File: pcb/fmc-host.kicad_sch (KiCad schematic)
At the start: 309 parts, among them J1 SMA002, J10 BM08B-SURS-TF, J2 SMA002, J3 SMA002, J4 SMA002, J5 SMA002, J6 FTSH-105-01-F-D-RA-K, J7 12226-8250-00FR, J8 FMC_SINGLE_WIDTH_MODULE, J9 ASP-134488-01, Q1 SI1012R, Q2 SI1012R, U1 SN74LVC2G34DCKR, U10 DS90UB934-Q1, U11 DS91M040, U12 AD5766BCPZ-RL7, U13 MCP47FEB02A0-E/ST, U14 LM4132AMF-2.5/NOPBCT-ND, U15 AD7616BSTZ, U16 AD5142BCPZ10, U17 LTM4622A, U18 D3V3XA4B10LP, U19 TPS7A49, U2 SN65LVDS9638DGN, U20 TPS7A49, U21 TPS7A30, U22 24ST, U23 LTM8049_BGA, U24 TPS62061DSGT, U25 D3V3XA4B10LP, U26 D3V3XA4B10LP, U3 FIN1032MTCX, U4 ADCMP600, U5 ADCMP600, U6 DG1412E, U7 DG1412E, U8 DG1412E, U9 DS90UB934-Q1, X2 OE-LOGO_7X5

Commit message: Added OEPS PN
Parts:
- C1, C106, C118, C139, C140, C2, C26, C27, C34, C35, C36, C37, C5, C6, C70, C71, C72, C73, C79, C80, C81, C91, C92: MPN (none) -> GRM31CR71E106KA12L; OEPS PN (none) -> OEPS M05 035; old description (none) -> CAP CER 1206 10uF 25V ±10% X7R
- C10, C100, C104, C107, C110, C111, C112, C114, C115, C13, C132, C134, C135, C137, C138, C14, C15, C16, C17, C18, C19, C22, C23, C3, C30, C31, C32, C33, C4, C41, C43, C44, C45, C46, C47, C48, C49, C52, C53, C54, C55, C56, C60, C61, C63, C65, C67, C68, C7, C78, C8, C83, C84, C85, C86, C87, C89, C9, C90, C93, C99: MPN (none) -> GRM155R71E104KE14D; OEPS PN (none) -> OEPS M05 032; old description (none) -> CAP CER 0402 100nF 25V ±10% X7R
- C101, C103, C105, C108, C109, C113, C116, C117, C119, C120, C121, C125, C126, C127, C59, C62, C69, C77, C95, C96: MPN (none) -> GRM21BR61E106KA73L; OEPS PN (none) -> OEPS M05 034; old description (none) -> CAP CER 0805 10uF 25V ±10% X5R
- C102, C130, C131, C94, C97, C98: MPN (none) -> TMK325ABJ476MM-T; OEPS PN (none) -> OEPS M05 036; old description (none) -> CAP CER 1210 47uF 25V ±20% X5R
- C11, C12, C122, C123, C124, C20, C21, C24, C25, C50, C51, C57, C58, C82: MPN (none) -> GCM155R71E103KA37D; OEPS PN (none) -> OEPS M05 030; old description (none) -> CAP CER 0402 10nF 25V ±10% X7R
- C128, C129: MPN (none) -> C1210C104KCRAC7800; OEPS PN (none) -> OEPS M05 072; old description (none) -> CAP CER 1210 100nF 500V ±10% X7R
- C133, C136: MPN (none) -> TL8B0336M020C; OEPS PN (none) -> OEPS M05 073; old description (none) -> CAP TAN 1411 33uF 20V ±20% B0
- C28, C29: MPN (none) -> CC0402KRX7R8BB472; OEPS PN (none) -> OEPS M05 029; old description (none) -> CAP CER 0402 4.7nF 25V ±10% X7R
- C38, C39: MPN (none) -> GRM155R71E473KA88D; OEPS PN (none) -> OEPS M05 031; old description (none) -> CAP CER 0402 47nF 25V ±10% X7R
- C40, C42, C64, C66, C74, C75, C76, C88: MPN (none) -> GCM21BR71E105KA56L; OEPS PN (none) -> OEPS M05 033; old description (none) -> CAP CER 0805 1uF 25V ±10% X7R
- D1, D2: MPN (none) -> SESD0402X1UN-0030-088; OEPS PN (none) -> OEPS M05 043; old description (none) -> TVS Diode 0402
- D3, D4, D5: MPN (none) -> BAR 66 E6327; OEPS PN (none) -> OEPS M05 044; old description (none) -> PIN Diode STO23
- D6: MPN (none) -> KDZVTR4.3B; OEPS PN (none) -> OEPS M05 045; old description (none) -> Zener Diode SOD123
- F1, F2, F3: MPN (none) -> MINISMDC014F-2; OEPS PN (none) -> OEPS M05 008; old description (none) -> Polyfuse
- J1, J2, J3, J4, J5: MPN (none) -> 6-1634010-0; OEPS PN (none) -> OEPS M05 001; old description (none) -> MMCX Coax Connector
- J10: MPN (none) -> BM08B-SURS-TF; OEPS PN (none) -> OEPS M05 076; old description (none) -> Connector header 8POS 0.8mm
- J6: MPN (none) -> FTSH-105-01-F-D-RA-K; OEPS PN (none) -> OEPS M05 077; old description (none) -> Connector header RA 10POS 1.27mm
- J7: MPN (none) -> 12226-8250-00FR; OEPS PN (none) -> OEPS M05 003; old description (none) -> SDR Cable Receptacle
- J8, TP1, TP10, TP11, TP12, TP13, TP14, TP15, TP16, TP17, TP18, TP2, TP3, TP4, TP5, TP6, TP7, TP8, TP9, X2: now not fitted; now left out of the parts list
- J9: MPN (none) -> ASP-134488-01; OEPS PN (none) -> OEPS M05 005; old description (none) -> FMC HPC Male Connector
- L1, L2: MPN (none) -> 1008PS-472KLB; OEPS PN (none) -> OEPS M05 037; old description (none) -> Inductor
- L10, L11, L12, L3, L4, L9: MPN (none) -> BLM18KG601SN1D; OEPS PN (none) -> OEPS M05 038; old description (none) -> Inductor 063
- L13: MPN (none) -> 1277AS-H-6R8M=P2; OEPS PN (none) -> OEPS M05 075; old description (none) -> Inductor 1210
- L14, L15, L16, L17, L18, L19: MPN (none) -> BLM15PX601SN1D; OEPS PN (none) -> OEPS M05 041; PARTNO BLM15PX601SN1D -> (none); old description (none) -> Inductor 0402
- L5, L6: MPN (none) -> SRN6045TA-101M; OEPS PN (none) -> OEPS M05 039; old description (none) -> Inductor
- L7, L8: MPN (none) -> MPZ2012S102AT000; OEPS PN (none) -> OEPS M05 040; old description (none) -> Inductor 0805
- Q1, Q2: MPN (none) -> SI1012R-T1-GE3; OEPS PN (none) -> OEPS M05 047; old description (none) -> N MOSFET
- R1, R2, R38, R39: MPN (none) -> ERJ-2RKF3001X; OEPS PN (none) -> OEPS M05 017; old description (none) -> RES SMD 0402 3kΩ ±1% 0.100W
- R10, R3, R4, R57, R58, R9: MPN (none) -> ERJ-2RKF2001X; OEPS PN (none) -> OEPS M05 015; old description (none) -> RES SMD 0402 2kΩ ±1% 0.100W
- R11, R12, R5, R6, R7, R8: MPN (none) -> CRGP0603F150R; OEPS PN (none) -> OEPS M05 013; old description (none) -> RES SMD 0603 150Ω ±1% 0.250W
- R13, R14, R49, R50, R51, R52, R76: MPN (none) -> ERJ-2RKF1653X; OEPS PN (none) -> OEPS M05 026; old description (none) -> RES SMD 0402 165kΩ ±1% 0.100W
- R15, R16, R35, R37, R59, R63, R64, R65, R66, R67, R68, R78, R79: MPN (none) -> ERJ-2RKF1002X; OEPS PN (none) -> OEPS M05 021; old description (none) -> RES SMD 0402 10kΩ ±1% 0.100W
- R17, R18, R41, R42, R44, R45, R46, R47: MPN (none) -> ERJ-2RKF1001X; OEPS PN (none) -> OEPS M05 014; old description (none) -> RES SMD 0402 1kΩ ±1% 0.100W
- R19, R21: MPN (none) -> ERJ-2RKF5601X; OEPS PN (none) -> OEPS M05 020; old description (none) -> RES SMD 0402 5.6kΩ ±1% 0.100W
- R20, R22: MPN (none) -> ERJ-2RKF2102X; OEPS PN (none) -> OEPS M05 023; old description (none) -> RES SMD 0402 21kΩ ±1% 0.100W
- R23, R24, R28, R29: MPN (none) -> RR0510R-49R9-D; OEPS PN (none) -> OEPS M05 010; old description (none) -> RES SMD 0402 49.9Ω ±0.5% 0.063W
- R25, R26, R27: MPN (none) -> ERJ-2RKF1000X; OEPS PN (none) -> OEPS M05 012; old description (none) -> RES SMD 0402 100Ω ±1% 0.100W
- R30, R31, R32, R33, R40, R43, R71, R73, R75: MPN (none) -> ERJ-2RKF4701X; OEPS PN (none) -> OEPS M05 019; old description (none) -> RES SMD 0402 4.7kΩ ±1% 0.100W
- R34, R36: MPN (none) -> R34, R36; OEPS PN (none) -> OEPS000000; now not fitted
- R48: MPN (none) -> RC0402JR-070RL; OEPS PN (none) -> OEPS M05 009; old description (none) -> RES SMD 0402 0Ω 1A
- R53, R54, R55, R56: MPN (none) -> EXB-2HV222JV; OEPS PN (none) -> OEPS M05 016; old description (none) -> 2.2k IC
- R60, R61: MPN (none) -> ERJ-2RKF3481X; OEPS PN (none) -> OEPS M05 018; old description (none) -> RES SMD 0402 3.48kΩ ±1% 0.100W
- R62: MPN (none) -> ERJ-2RKF6493X; OEPS PN (none) -> OEPS M05 028; old description (none) -> RES SMD 0402 649kΩ ±1% 0.100W
- R69: MPN (none) -> ERJ-2RKF2201X; OEPS PN (none) -> OEPS M05 074; old description (none) -> RES SMD 0402 2.2kΩ ±1% 0.100W
- R70: MPN (none) -> ERJ-2RKF1502X; OEPS PN (none) -> OEPS M05 022; old description (none) -> RES SMD 0402 15kΩ ±1% 0.100W
- R72, R74: MPN (none) -> ERJ-2RKF4702X; OEPS PN (none) -> OEPS M05 070; old description (none) -> RES SMD 0402 47kΩ ±1% 0.100W
- R77: MPN (none) -> ERJ-2RKF1783X; OEPS PN (none) -> OEPS M05 027; old description (none) -> RES SMD 0402 178kΩ ±1% 0.100W
- R80, R81: MPN (none) -> ERJ-2RKF7322X; OEPS PN (none) -> OEPS M05 025; old description (none) -> RES SMD 0402 73.2kΩ ±1% 0.100W
- S1, S2: MPN (none) -> CHS-01TA; OEPS PN (none) -> OEPS M05 006; old description (none) -> DIP Switch; now not fitted
- S3: MPN (none) -> CHS-02TB; OEPS PN (none) -> OEPS M05 007; old description (none) -> DIP Switch
- U1: MPN (none) -> SN74LVC2G34DCKR; OEPS PN (none) -> OEPS M05 048; old description (none) -> Logic Buffer
- U10, U9: MPN (none) -> DS90UB934TRGZRQ1; OEPS PN (none) -> OEPS M05 071; old description (none) -> Deserializer
- U11: MPN (none) -> DS91M040TSQ/NOPB; OEPS PN (none) -> OEPS M05 055; old description (none) -> Quad M-LVDS Transceiver
- U12: MPN (none) -> AD5766BCPZ-RL7; OEPS PN (none) -> OEPS M05 056; old description (none) -> 16 Channel DAC
- U13: MPN (none) -> MCP47FEB02A0-E/ST; OEPS PN (none) -> OEPS M05 057; old description (none) -> 8-bit 2 channel DAC
- U14: MPN (none) -> LM4132AMF-2.5/NOPBCT-ND; OEPS PN (none) -> OEPS M05 058; old description (none) -> 2.5V Reference
- U15: MPN (none) -> AD7616BSTZ; OEPS PN (none) -> OEPS080205; old description (none) -> ADC 16BIT 16 channels
- U16: MPN (none) -> AD5142BRUZ10; OEPS PN (none) -> OEPS080118; old description (none) -> Digital Potentiometer
- U17: MPN (none) -> LTM4622AIY#PBF; OEPS PN (none) -> OEPS M05 061; old description (none) -> DC-DC Converter
- U18, U25, U26: MPN (none) -> D3V3XA4B10LP-7; OEPS PN (none) -> OEPS080204; old description (none) -> TVS DIODE ARRAY
- U19, U20: MPN (none) -> TPS7A4901DRBR; OEPS PN (none) -> OEPS M05 062; old description (none) -> Positive LDO Regulator
- U2: MPN (none) -> SN65LVDS9638DGN; OEPS PN (none) -> OEPS M05 049; old description (none) -> Quad LVDS Driver
- U21: MPN (none) -> TPS7A3001DRBT; OEPS PN (none) -> OEPS M05 063; old description (none) -> Negative LDO Regulator
- U22: MPN (none) -> 24AA64-I/ST; OEPS PN (none) -> OEPS M05 064; old description (none) -> EEPROM
- U23: MPN (none) -> LTM8049IY#PBF; OEPS PN (none) -> OEPS M05 065; old description (none) -> DC-DC Converter
- U24: MPN (none) -> TPS62061DSGT; OEPS PN (none) -> OEPS M05 078; old description (none) -> Step Down Converter 1.8V 1.6A
- U3: MPN (none) -> FIN1032MTCX; OEPS PN (none) -> OEPS M05 050; old description (none) -> Quad LVDS Receiver
- U4, U5: MPN (none) -> ADCMP600BRJZ-R2; OEPS PN (none) -> OEPS M05 052; old description (none) -> Comparitor
- U6, U7, U8: MPN (none) -> DG1412EEN-T1-GE4; OEPS PN (none) -> OEPS M05 053; old description (none) -> Quad SPST

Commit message: Updated to latest OEPS PN and upgraded to KiCad 10
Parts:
- C1, C106, C118, C139, C140, C2, C26, C27, C34, C35, C36, C37, C5, C6, C70, C71, C72, C73, C79, C80, C81, C91, C92: OEPS PN OEPS M05 035 -> OEPS010007; old description CAP CER 1206 10uF 25V ±10% X7R -> CAPACITOR: SMD CER 1206 10uF 25V ±10% X7R [GRM31CR71E106KA1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
- C10, C100, C104, C107, C110, C111, C112, C114, C115, C13, C132, C134, C135, C137, C138, C14, C15, C16, C17, C18, C19, C22, C23, C3, C30, C31, C32, C33, C4, C41, C43, C44, C45, C46, C47, C48, C49, C52, C53, C54, C55, C56, C60, C61, C63, C65, C67, C68, C7, C78, C8, C83, C84, C85, C86, C87, C89, C9, C90, C93, C99: OEPS PN OEPS M05 032 -> OEPS010004; old description CAP CER 0402 100nF 25V ±10% X7R -> CAPACITOR: SMD CER 0402 100nF 25V ±10% X7R [GRM155R71E104KE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
- C101, C103, C105, C108, C109, C113, C116, C117, C119, C120, C121, C125, C126, C127, C59, C62, C69, C77, C95, C96: OEPS PN OEPS M05 034 -> OEPS010006; old description CAP CER 0805 10uF 25V ±10% X5R -> CAPACITOR: SMD CER 0805 10uF 25V ±10% X5R [GRM21BR61E106KA7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
- C102, C130, C131, C94, C97, C98: OEPS PN OEPS M05 036 -> OEPS010008; old description CAP CER 1210 47uF 25V ±20% X5R -> CAPACITOR: SMD CER 1210 47uF 25V ±20% X5R [TMK325ABJ476MM-T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
- C11, C12, C122, C123, C124, C20, C21, C24, C25, C50, C51, C57, C58, C82: OEPS PN OEPS M05 030 -> OEPS010002; old description CAP CER 0402 10nF 25V ±10% X7R -> CAPACITOR: SMD CER 0402 10nF 25V ±10% X7R [GCM155R71E103KA3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
- C128, C129: MPN C1210C104KCRAC7800 -> C1210C104KCRACTU; OEPS PN OEPS M05 072 -> OEPS010091; old description CAP CER 1210 100nF 500V ±10% X7R -> CAPACITOR: SMD CER 1210 100nF 500V ±10% X7R [C1210C104KCRAC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
- C133, C136: OEPS PN OEPS M05 073 -> OEPS210010; old description CAP TAN 1411 33uF 20V ±20% B0 -> CAPACITOR POL: SMD TANT B0 1411 33uF 20V ±20% 50Ohm [TL8B03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
- C28, C29: OEPS PN OEPS M05 029 -> OEPS010001; old description CAP CER 0402 4.7nF 25V ±10% X7R -> CAPACITOR: SMD CER 0402 4.7nF 25V ±10% X7R [CC0402KRX7R8BB4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
- C38, C39: OEPS PN OEPS M05 031 -> OEPS010003; old description CAP CER 0402 47nF 25V ±10% X7R -> CAPACITOR: SMD CER 0402 47nF 25V ±10% X7R [GRM155R71E473KA8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
- C40, C42, C64, C66, C74, C75, C76, C88: OEPS PN OEPS M05 033 -> OEPS010005; old description CAP CER 0805 1uF 25V ±10% X7R -> CAPACITOR: SMD CER 0805 1uF 25V ±10% X7R [GCM21BR71E105KA56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
- D1, D2: OEPS PN OEPS M05 043 -> OEPS030049; old description TVS Diode 0402 -> DIODE: TVS DIODE 7VWM 13VC [SESD0402X1UN-0030-088] [0402/2D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
- D3, D4, D5: MPN BAR 66 E6327 -> BAR66E6327HTSA1; OEPS PN OEPS M05 044 -> OEPS030050; old description PIN Diode STO23 -> #N/A
- D6: OEPS PN OEPS M05 045 -> OEPS030051; old description Zener Diode SOD123 -> DIODE: DIODE ZENER 4.55V 1W [KDZVTR4.3B] [PMDU]
- F1, F2, F3: OEPS PN OEPS M05 008 -> OEPS100088; old description Polyfuse -> OTHER: PTC RESET FUSE 60V 140MA 1812 [MINISMDC014F-2] [Othe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
- J1, J2, J3, J4, J5: OEPS PN OEPS M05 001 -> OEPS070003; old description MMCX Coax Connector -> CONNECTOR: MMCX RCPT 50ohm 90º [6-1634010-0] [TH]
- J10: OEPS PN OEPS M05 076 -> OEPS070149; old description Connector header 8POS 0.8mm -> CONNECTOR: HEADER 0.8MM 8POS [BM08B-SURS-TF] [SMD]
- J6: OEPS PN OEPS M05 077 -> OEPS070147; old description Connector header RA 10POS 1.27mm -> CONNECTOR: HEADER 1.27MM R/A 10POS [FTSH-105-01-F-D-RA-K] [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
- J7: OEPS PN OEPS M05 003 -> OEPS070009; old description SDR Cable Receptacle -> CONNECTOR: SDR RCPT 90º 26POS [12226-8250-00FR] [SMD]
- J9: OEPS PN OEPS M05 005 -> OEPS070148; old description FMC HPC Male Connector -> CONNECTOR: ARRAY PLUG 400POS GOLD [ASP-134488-01] [SMD]
- L1, L2: OEPS PN OEPS M05 037 -> OEPS040032; old description Inductor -> INDUCTOR: FIXED INDUCTOR SMD 4.7uH 950mA 350mΩ [1008PS-472K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
- L10, L11, L12, L3, L4, L9: OEPS PN OEPS M05 038 -> OEPS040029; old description Inductor 063 -> INDUCTOR: FERRITE BEAD SMD 0603 600Ω 1.3A 150mΩ (OEPS J30 0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
- L13: OEPS PN OEPS M05 075 -> OEPS040035; old description Inductor 1210 -> INDUCTOR: FIXED INDUCTOR SMD 6.8uH 1.2A 276mΩ [1277AS-H-6R8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
- L14, L15, L16, L17, L18, L19: OEPS PN OEPS M05 041 -> OEPS040019; old description Inductor 0402 -> INDUCTOR: FERRITE BEAD SMD 0402 600Ω 900mA 230mΩ [BLM15PX60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
- L5, L6: OEPS PN OEPS M05 039 -> OEPS040033; old description Inductor -> INDUCTOR: FIXED INDUCTOR SMD 100uH 920mA 456mΩ [SRN6045TA-1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
- L7, L8: OEPS PN OEPS M05 040 -> OEPS040034; old description Inductor 0805 -> INDUCTOR: FERRITE BEAD SMD 0805 1kΩ 1.5A 150mΩ [MPZ2012S102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
- Q1, Q2: OEPS PN OEPS M05 047 -> OEPS060001; old description N MOSFET -> TRANSISTOR: MOSFET N-CH 20V 500mA [SI1012R-T1-GE3] [SC-75A]
- R1, R2, R38, R39: OEPS PN OEPS M05 017 -> OEPS020008; old description RES SMD 0402 3kΩ ±1% 0.100W -> RESISTOR: SMD 0402 3kΩ ±1% 0.100W [ERJ-2RKF3001X] [SMD]
- R10, R3, R4, R57, R58, R9: OEPS PN OEPS M05 015 -> OEPS020007; old description RES SMD 0402 2kΩ ±1% 0.100W -> RESISTOR: SMD 0402 2kΩ ±1% 0.100W [ERJ-2RKF2001X] [SMD]
- R11, R12, R5, R6, R7, R8: OEPS PN OEPS M05 013 -> OEPS020023; old description RES SMD 0603 150Ω ±1% 0.250W -> RESISTOR: SMD 0603 150Ω ±1% 0.250W [CRGP0603F150R] [SMD]
- R13, R14, R49, R50, R51, R52, R76: OEPS PN OEPS M05 026 -> OEPS020020; old description RES SMD 0402 165kΩ ±1% 0.100W -> RESISTOR: SMD 0402 165kΩ ±1% 0.100W [ERJ-2RKF1653X] [SMD]
- R15, R16, R35, R37, R59, R63, R64, R65, R66, R67, R68, R78, R79: OEPS PN OEPS M05 021 -> OEPS020013; old description RES SMD 0402 10kΩ ±1% 0.100W -> RESISTOR: SMD 0402 10kΩ ±1% 0.100W [ERJ-2RKF1002X] [SMD]
- R17, R18, R41, R42, R44, R45, R46, R47: OEPS PN OEPS M05 014 -> OEPS020006; old description RES SMD 0402 1kΩ ±1% 0.100W -> RESISTOR: SMD 0402 1kΩ ±1% 0.100W [ERJ-2RKF1001X] [SMD]
- R19, R21: OEPS PN OEPS M05 020 -> OEPS020011; old description RES SMD 0402 5.6kΩ ±1% 0.100W -> RESISTOR: SMD 0402 5.6kΩ ±1% 0.100W [ERJ-2RKF5601X] [SMD]
- R20, R22: OEPS PN OEPS M05 023 -> OEPS020016; old description RES SMD 0402 21kΩ ±1% 0.100W -> RESISTOR: SMD 0402 21kΩ ±1% 0.100W [ERJ-2RKF2102X] [SMD]
- R23, R24, R28, R29: OEPS PN OEPS M05 010 -> OEPS020002; old description RES SMD 0402 49.9Ω ±0.5% 0.063W -> RESISTOR: SMD 0402 49.9Ω ±0.5% 0.063W [RR0510R-49R9-D] [SMD]
- R25, R26, R27: OEPS PN OEPS M05 012 -> OEPS020004; old description RES SMD 0402 100Ω ±1% 0.100W -> RESISTOR: SMD 0402 100Ω ±1% 0.100W [ERJ-2RKF1000X] [SMD]
- R30, R31, R32, R33, R40, R43, R71, R73, R75: OEPS PN OEPS M05 019 -> OEPS020010; old description RES SMD 0402 4.7kΩ ±1% 0.100W -> RESISTOR: SMD 0402 4.7kΩ ±1% 0.100W [ERJ-2RKF4701X] [SMD]
- R34, R36: MPN R34, R36 -> -
- R48: OEPS PN OEPS M05 009 -> OEPS020001; old description RES SMD 0402 0Ω 1A -> RESISTOR: SMD 0402 0Ω 1A [RC0402JR-070RL] [SMD]
- R53, R54, R55, R56: OEPS PN OEPS M05 016 -> OEPS080206; old description 2.2k IC -> IC: RES ARRAY 8 RES 2.2K OHM 1506 [EXB-2HV222JV] [SMD]
- R60, R61: OEPS PN OEPS M05 018 -> OEPS020009; old description RES SMD 0402 3.48kΩ ±1% 0.100W -> RESISTOR: SMD 0402 3.48kΩ ±1% 0.100W [ERJ-2RKF3481X] [SMD]
- R62: OEPS PN OEPS M05 028 -> OEPS020022; old description RES SMD 0402 649kΩ ±1% 0.100W -> RESISTOR: SMD 0402 649kΩ ±1% 0.100W [ERJ-2RKF6493X] [SMD]
- R69: OEPS PN OEPS M05 074 -> OEPS020174; old description RES SMD 0402 2.2kΩ ±1% 0.100W -> RESISTOR: SMD 0402 2.2kΩ ±1% 0.100W [ERJ-2RKF2201X] [SMD]
- R70: OEPS PN OEPS M05 022 -> OEPS020015; old description RES SMD 0402 15kΩ ±1% 0.100W -> RESISTOR: SMD 0402 15kΩ ±1% 0.100W [ERJ-2RKF1502X] [SMD]
- R72, R74: OEPS PN OEPS M05 070 -> OEPS020017; old description RES SMD 0402 47kΩ ±1% 0.100W -> RESISTOR: SMD 0402 47kΩ ±1% 0.100W [ERJ-2RKF4702X] [SMD]
- R77: OEPS PN OEPS M05 027 -> OEPS020021; old description RES SMD 0402 178kΩ ±1% 0.100W -> RESISTOR: SMD 0402 178kΩ ±1% 0.100W [ERJ-2RKF1783X] [SMD]
- R80, R81: OEPS PN OEPS M05 025 -> OEPS020018; old description RES SMD 0402 73.2kΩ ±1% 0.100W -> RESISTOR: SMD 0402 73.2kΩ ±1% 0.100W [ERJ-2RKF7322X] [SMD]
- S1, S2: OEPS PN OEPS M05 006 -> OEPS100086; old description DIP Switch -> OTHER: SWITCH SLIDE DIP SPST 0.1A 6V 1 POS [CHS-01TA] [Othe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
- S3: OEPS PN OEPS M05 007 -> OEPS100087; old description DIP Switch -> OTHER: SWITCH SLIDE DIP SPST 0.1A 6V 2 POS [CHS-02TB] [Othe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
- U1: OEPS PN OEPS M05 048 -> OEPS080207; old description Logic Buffer -> IC: BUFFER NON-INVERT 2CH [SN74LVC2G34DCKR] [SC-70-6]
- U10, U9: OEPS PN OEPS M05 071 -> OEPS080210; old description Deserializer -> IC: DESERIALIZER FPD-Link III [DS90UB934TRGZRQ1] [48-VQFN (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
- U11: OEPS PN OEPS M05 055 -> OEPS080211; old description Quad M-LVDS Transceiver -> IC: TRANSCEIVER Half LVDS [DS91M040TSQ/NOPB] [32-WQFN (5x5)]
- U12: OEPS PN OEPS M05 056 -> OEPS080212; old description 16 Channel DAC -> IC: DAC 16BIT 16CH [AD5766BCPZ-RL7] [40-LFCSP-WQ (6x6)]
- U13: OEPS PN OEPS M05 057 -> OEPS080213; old description 8-bit 2 channel DAC -> IC: DAC 8BIT 2CH [MCP47FEB02A0-E/ST] [8-TSSOP]
- U14: MPN LM4132AMF-2.5/NOPBCT-ND -> LM4132AMF-2.5/NOPB; OEPS PN OEPS M05 058 -> OEPS080214; old description 2.5V Reference -> IC: VREF 2.5V 0.05% [LM4132AMF-2.5/NOPB] [SOT-23-5]
- U15: old description ADC 16BIT 16 channels -> IC: ADC 16BIT 16 channels [AD7616BSTZ] [80-LQFP]
- U16: old description Digital Potentiometer -> IC: DGT POT 10KOHM 256TAP 16TSSOP [AD5142BRUZ10] [16-TSSOP]
- U17: OEPS PN OEPS M05 061 -> OEPS080003; old description DC-DC Converter -> IC: DC-DC CONVERTER 2outputs1.5-12V 1.5-12V [LTM4622AIY#PBF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
- U18, U25, U26: old description TVS DIODE ARRAY -> IC: TVS DIODE ARRAY [D3V3XA4B10LP-7] [10-UFDFN]
- U19, U20: OEPS PN OEPS M05 062 -> OEPS080215; old description Positive LDO Regulator -> IC: LDO ADJ 150mA [TPS7A4901DRBR] [8-SON (3x3)]
- U2: OEPS PN OEPS M05 049 -> OEPS080007; old description Quad LVDS Driver -> IC: LVDS 2channel driver [SN65LVDS9638DGN] [8-MSOP-PowerPad]
- U21: OEPS PN OEPS M05 063 -> OEPS080216; old description Negative LDO Regulator -> IC: LDO NEGATIVE ADJ 200mA [TPS7A3001DRBT] [8-SON (3x3)]
- U22: OEPS PN OEPS M05 064 -> OEPS080217; old description EEPROM -> IC: EEPROM 64KBIT I2C [24AA64-I/ST] [8-TSSOP]
- U23: OEPS PN OEPS M05 065 -> OEPS080218; old description DC-DC Converter -> IC: DC DC CONVERTER ADJ 2outputs 2x1A [LTM8049IY#PBF] [77-B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
- U24: OEPS PN OEPS M05 078 -> OEPS080219; old description Step Down Converter 1.8V 1.6A -> IC: FIXED REG BUCK 1.8V 1.6A [TPS62061DSGT] [8-WSON (2x2)]
- U3: OEPS PN OEPS M05 050 -> OEPS080006; old description Quad LVDS Receiver -> IC: LVDS 4channel receiver [FIN1032MTCX] [16-TSSOP]
- U4, U5: OEPS PN OEPS M05 052 -> OEPS080208; old description Comparitor -> IC: COMPARATOR 1 GP [ADCMP600BRJZ-R2] [SOT23-5]
- U6, U7, U8: OEPS PN OEPS M05 053 -> OEPS080209; old description Quad SPST -> IC: SWITCH SPST-NOX4 1.5OHM [DG1412EEN-T1-GE4] [16-QFN (4x4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

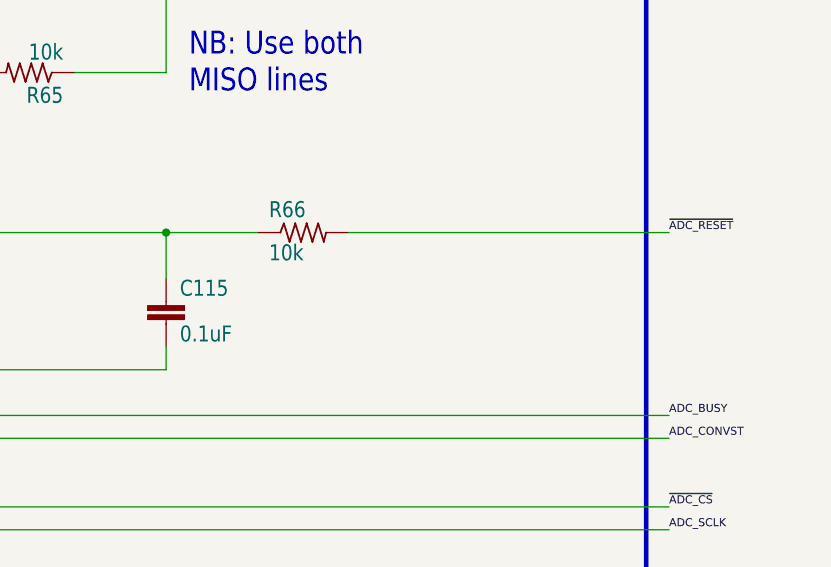
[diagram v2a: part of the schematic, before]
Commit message: Fix AD761x nRESET input
- Replace 0.1uF filter capacitor with 100pF
- Replace series 10k resistor with 0 ohm jumper
- Add 10k pulldown so that chip power-on defaults to the reset state
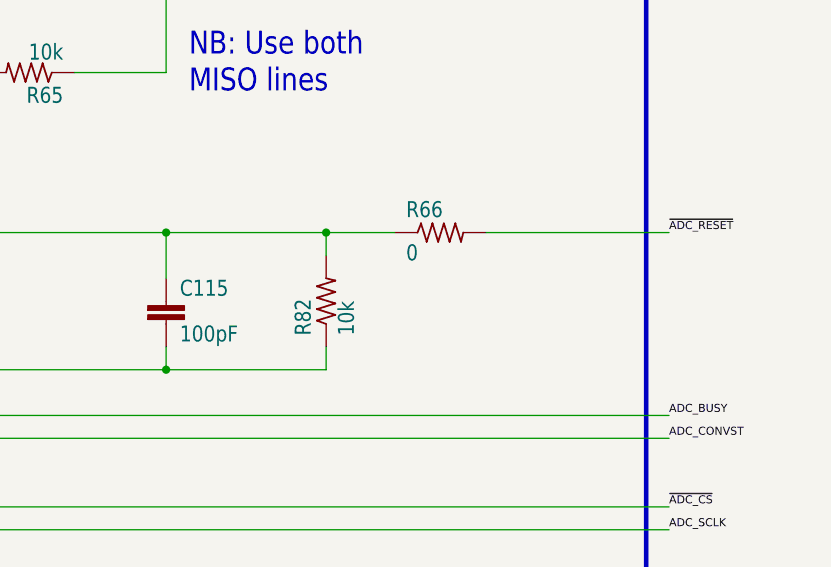
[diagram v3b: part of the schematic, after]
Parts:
- added R82: 10k, fmc-host:0402, symbol fmc-host-eagle-import:R_0402
- C115: value 0.1uF -> 100pF; MPN GRM155R71E104KE14D -> (none); OEPS PN OEPS010004 -> (none); old description CAPACITOR: SMD CER 0402 100nF 25V ±10% X7R [GRM155R71E104KE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 -> (none)
- R66: value 10k -> 0; MPN ERJ-2RKF1002X -> (none); OEPS PN OEPS020013 -> (none); old description RESISTOR: SMD 0402 10kΩ ±1% 0.100W [ERJ-2RKF1002X] [SMD] -> (none)
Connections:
- net GND: now also R82.1
- net at C115.1, R66.1, U15.36 (~{RESET}): now also R82.2
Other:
- moved on the sheet: R66
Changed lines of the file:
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@@
 	)
 	(junction
-		(at 579.12 408.94)
-		(diameter 0)
-		(color 0 0 0 0)
-	)
-	(junction
 		(at 185.42 403.86)
 		(diameter 0)
@@
 	)
 	(junction
+		(at 579.12 424.18)
+		(diameter 0)
+		(color 0 0 0 0)
+	)
+	(junction
 		(at 340.36 1229.36)
 		(diameter 0)
@@
 	)
 	(junction
+		(at 596.9 408.94)
+		(diameter 0)
+		(color 0 0 0 0)
+	)
+	(junction
 		(at 706.12 203.2)
 		(diameter 0)
@@
 	)
 	(junction
+		(at 579.12 408.94)
+		(diameter 0)
+		(color 0 0 0 0)
+	)
+	(junction
 		(at 571.5 810.26)
 		(diameter 0)
@@
 	(wire
 		(pts
+			(xy 596.9 424.18) (xy 596.9 421.64)
+		)
+		(stroke
+			(width 0.1524)
+			(type solid)
+		)
+	)
+	(wire
+		(pts
 			(xy 256.54 421.64) (xy 256.54 533.4)
 		)
@@
 	(wire
 		(pts
-			(xy 579.12 408.94) (xy 589.28 408.94)
+			(xy 579.12 408.94) (xy 596.9 408.94)
 		)
 		(stroke
@@
 	(wire
 		(pts
+			(xy 579.12 424.18) (xy 596.9 424.18)
+		)
+		(stroke
+			(width 0.1524)
+			(type solid)
+		)
+	)
+	(wire
+		(pts
 			(xy 170.18 764.54) (xy 170.18 754.38)
 		)
@@
 	(wire
 		(pts
-			(xy 635 408.94) (xy 599.44 408.94)
+			(xy 635 408.94) (xy 614.68 408.94)
 		)
 		(stroke
@@
 	(wire
 		(pts
+			(xy 596.9 408.94) (xy 604.52 408.94)
+		)
+		(stroke
+			(width 0.1524)
+			(type solid)
+		)
+	)
+	(wire
+		(pts
 			(xy 744.22 746.76) (xy 734.06 746.76)
 		)
@@
 	(wire
 		(pts
+			(xy 596.9 411.48) (xy 596.9 408.94)
+		)
+		(stroke
+			(width 0.1524)
+			(type solid)
+		)
+	)
+	(wire
+		(pts
 			(xy 683.26 99.06) (xy 685.8 99.06)
 		)
@@
 	)
 	(symbol
+		(lib_id "fmc-host-eagle-import:R_0402")
+		(at 596.9 416.56 90)
+		(unit 1)
+		(body_style 1)
+		(exclude_from_sim no)
+		(in_bom yes)
+		(on_board yes)
+		(in_pos_files yes)
+		(dnp no)
+		(property "Reference" "R82"
+			(at 595.4014 420.37 0)
+			(show_name no)
+			(do_not_autoplace no)
+			(effects
+				(font
+					(size 1.778 1.5113)
+				)
+				(justify left bottom)
+			)
+		)
+		(property "Value" "10k"
+			(at 600.202 420.37 0)
+			(show_name no)
+			(do_not_autoplace no)
+			(effects
+				(font
+					(size 1.778 1.5113)
+				)
+				(justify left bottom)
+			)
+		)
+		(property "Footprint" "fmc-host:0402"
+			(at 596.9 416.56 0)
+			(hide yes)
+			(show_name no)
+			(do_not_autoplace no)
+			(effects
+				(font
+					(size 1.27 1.27)
+				)
+			)
+		)
+		(property "Datasheet" ""
+			(at 596.9 416.56 0)
+			(hide yes)
+			(show_name no)
+			(do_not_autoplace no)
+			(effects
+				(font
+					(size 1.27 1.27)
+				)
+			)
+		)
+		(property "Description" ""
+			(at 596.9 416.56 0)
+			(hide yes)
+			(show_name no)
+			(do_not_autoplace no)
+			(effects
+				(font
+					(size 1.27 1.27)
+				)
+			)
+		)
+		(property "MPN" "ERJ-2RKF1002X"
+			(at 596.9 416.56 0)
+			(hide yes)
+			(show_name no)
+			(do_not_autoplace no)
+			(effects
+				(font
+					(size 1.27 1.27)
+				)
+			)
+		)
+		(property "OEPS PN" "OEPS020013"
+			(at 596.9 416.56 0)
+			(hide yes)
+			(show_name no)
+			(do_not_autoplace no)
+			(effects
+				(font
+					(size 1.27 1.27)
+				)
+			)
+		)
+		(property "old description" "RESISTOR:   SMD 0402 10kΩ ±1% 0.100W   [ERJ-2RKF1002X] [SMD]"
+			(at 596.9 416.56 0)
+			(hide yes)
+			(show_name no)
+			(do_not_autoplace no)
+			(effects
+				(font
+					(size 1.27 1.27)
+				)
+			)
+		)
+		(pin "1"
+		)
+		(pin "2"
+		)
+		(instances
+			(project "fmc-host"
+				(path "/3a190272-84f9-4241-a964-a08ef93e1ba1"
+					(reference "R82")
+					(unit 1)
+				)
+			)
+		)
+	)
+	(symbol
 		(lib_id "fmc-host-eagle-import:GND")
 		(at 177.8 1148.08 0)
@@
 			)
 		)
-		(property "Value" "0.1uF"
+		(property "Value" "100pF"
 			(at 580.644 421.259 0)
 			(show_name no)
@@
 			)
 		)
-		(property "MPN" "GRM155R71E104KE14D"
+		(property "MPN" ""
 			(at 579.12 416.56 0)
 			(hide yes)
@@
 			)
 		)
-		(property "OEPS PN" "OEPS010004"
+		(property "OEPS PN" ""
 			(at 579.12 416.56 0)
 			(hide yes)
@@
 			)
 		)
-		(property "old description" "CAPACITOR:   SMD CER 0402 100nF 25V ±10% X7R   [GRM155R71E104KE14D] [SMD]"
+		(property "old description" ""
 			(at 579.12 416.56 0)
 			(hide yes)
@@
 	(symbol
 		(lib_id "fmc-host-eagle-import:R_0402")
-		(at 594.36 408.94 0)
+		(at 609.6 408.94 0)
 		(unit 1)
 		(body_style 1)
@@
 		(dnp no)
 		(property "Reference" "R66"
-			(at 590.55 407.4414 0)
+			(at 605.79 407.4414 0)
 			(show_name no)
 			(do_not_autoplace no)
@@
 			)
 		)
-		(property "Value" "10k"
-			(at 590.55 412.242 0)
+		(property "Value" "0"
+			(at 605.79 412.242 0)
 			(show_name no)
 			(do_not_autoplace no)
@@
 		)
 		(property "Footprint" "fmc-host:0402"
-			(at 594.36 408.94 0)
+			(at 609.6 408.94 0)
 			(hide yes)
 			(show_name no)
@@
 		)
 		(property "Datasheet" ""
-			(at 594.36 408.94 0)
+			(at 609.6 408.94 0)
 			(hide yes)
 			(show_name no)
@@
 		)
 		(property "Description" ""
-			(at 594.36 408.94 0)
+			(at 609.6 408.94 0)
 			(hide yes)
 			(show_name no)
@@
 			)
 		)
-		(property "MPN" "ERJ-2RKF1002X"
-			(at 594.36 408.94 0)
-			(hide yes)
-			(show_name no)
-			(do_not_autoplace no)
-			(effects
-				(font
-					(size 1.27 1.27)
-				)
-			)
-		)
-		(property "OEPS PN" "OEPS020013"
-			(at 594.36 408.94 0)
+		(property "MPN" ""
+			(at 609.6 408.94 0)
 			(hide yes)
 			(show_name no)
@@
 			)
 		)
-		(property "old description" "RESISTOR:   SMD 0402 10kΩ ±1% 0.100W   [ERJ-2RKF1002X] [SMD]"
-			(at 594.36 408.94 0)
+		(property "old description" ""
+			(at 609.6 408.94 0)
 			(hide yes)
 			(show_name no)
